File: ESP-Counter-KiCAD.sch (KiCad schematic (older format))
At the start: 37 parts, among them J1 Digital_IP, J2 Motor_Ctrl, J3 LED_Indicator, J5 24V_Input, K2 G2RL-1-DC24, K5 G2RL-1-DC24, U1 ESP_12E_J1, U10 VO615A, U2 ESP_12E_J2, U3 VO615A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

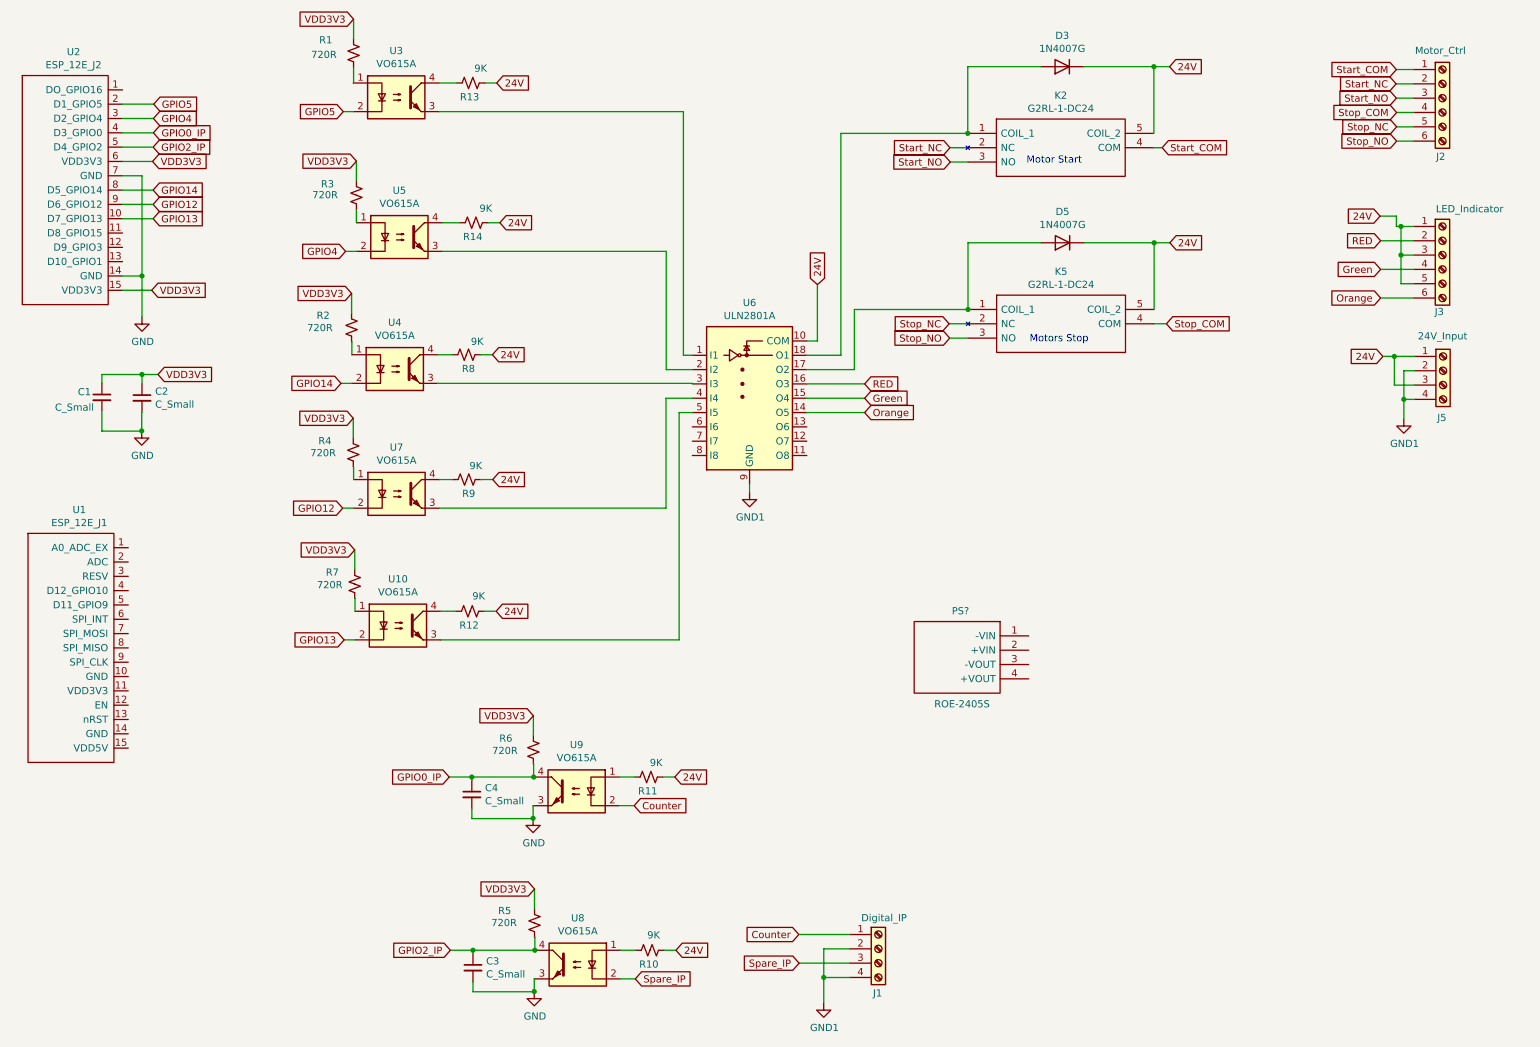
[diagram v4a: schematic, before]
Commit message: RECOM DCDC connections completed
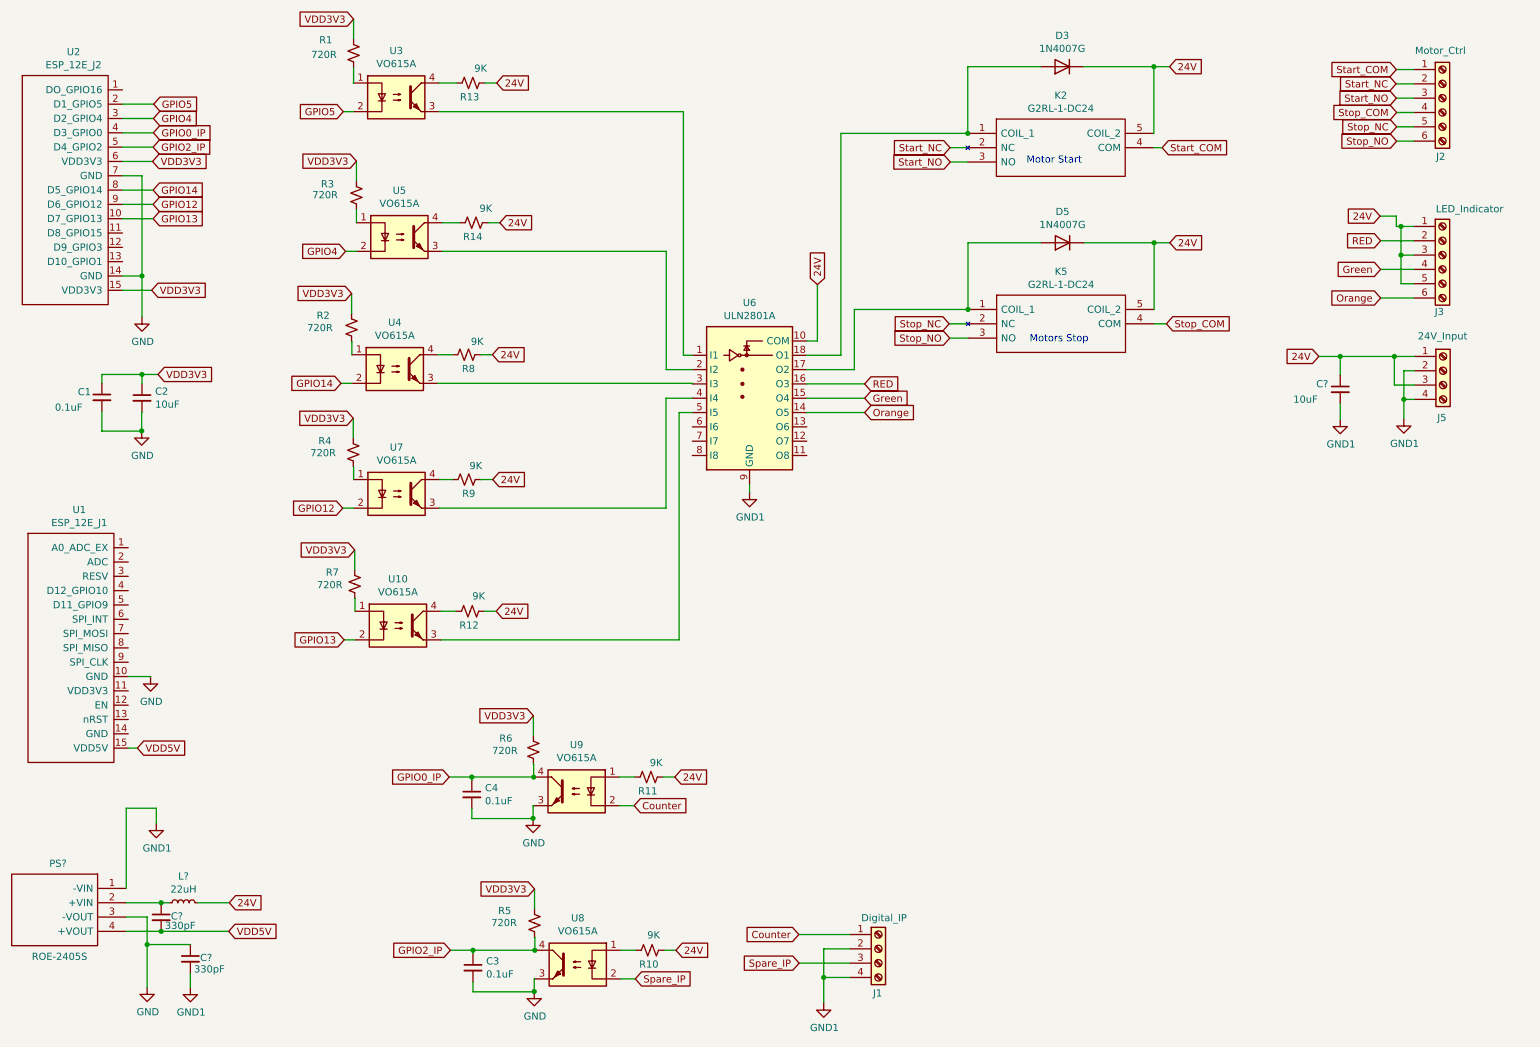
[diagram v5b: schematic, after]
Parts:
- added C?: 10uF, Capacitor_SMD:C_0603_1608Metric_Pad1.08x0.95mm_HandSolder, symbol Device:C_Small
- added C? (x2): 330pF, Capacitor_SMD:C_0603_1608Metric_Pad1.08x0.95mm_HandSolder, symbol Device:C_Small
- added L?: 22uH, symbol Device:L_Small
- C1, C3, C4: value C_Small -> 0.1uF
- C2: value C_Small -> 10uF
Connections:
- net labels added: VDD5V
- wire segments 152 -> 174
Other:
- moved on the sheet: PS?
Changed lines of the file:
@@
 P 1596 3302
 F 0 "C2" H 1688 3348 50  0000 L CNN
-F 1 "C_Small" H 1688 3257 50  0000 L CNN
+F 1 "10uF" H 1688 3257 50  0000 L CNN
 F 2 "Capacitor_SMD:C_0603_1608Metric_Pad1.08x0.95mm_HandSolder" H 1596 3302 50  0001 C CNN
 F 3 "~" H 1596 3302 50  0001 C CNN
@@
 P 1316 3298
 F 0 "C1" H 1148 3336 50  0000 L CNN
-F 1 "C_Small" H 988 3228 50  0000 L CNN
+F 1 "0.1uF" H 988 3228 50  0000 L CNN
 F 2 "Capacitor_SMD:C_0603_1608Metric_Pad1.08x0.95mm_HandSolder" H 1316 3298 50  0001 C CNN
 F 3 "~" H 1316 3298 50  0001 C CNN
@@
 	1    0    0    -1
 $EndComp
-Text GLabel 10264 3012 0    50   Input ~ 0
+Text GLabel 9816 3012 0    50   Input ~ 0
 24V
 Wire Wire Line
-	10264 3012 10344 3012
-Wire Wire Line
 	10484 3212 10344 3212
 Wire Wire Line
 	10344 3212 10344 3012
-Connection ~ 10344 3012
 Wire Wire Line
 	10344 3012 10484 3012
@@
 P 3900 6072
 F 0 "C4" H 3992 6118 50  0000 L CNN
-F 1 "C_Small" H 3992 6027 50  0000 L CNN
+F 1 "0.1uF" H 3992 6027 50  0000 L CNN
 F 2 "Capacitor_SMD:C_0603_1608Metric_Pad1.08x0.95mm_HandSolder" H 3900 6072 50  0001 C CNN
 F 3 "~" H 3900 6072 50  0001 C CNN
@@
 P 3908 7282
 F 0 "C3" H 4000 7328 50  0000 L CNN
-F 1 "C_Small" H 4000 7237 50  0000 L CNN
+F 1 "0.1uF" H 4000 7237 50  0000 L CNN
 F 2 "Capacitor_SMD:C_0603_1608Metric_Pad1.08x0.95mm_HandSolder" H 3908 7282 50  0001 C CNN
 F 3 "~" H 3908 7282 50  0001 C CNN
@@
 L ROE-2405S:ROE-2405S PS?
 U 1 1 601CB8A2
-P 7790 4964
-F 0 "PS?" H 8206 5138 50  0000 L CNN
-F 1 "ROE-2405S" H 8062 4488 50  0000 L CNN
-F 2 "ROE1205S" H 8640 5064 50  0001 L CNN
-F 3 "https://recom-power.com/pdf/Econoline/ROE.pdf" H 8640 4964 50  0001 L CNN
-F 4 "Recom Through Hole 1W Isolated DC-DC Converter, I/O isolation 1kV dc, Vout 5V dc" H 8640 4864 50  0001 L CNN "Description"
-F 5 "10.5" H 8640 4764 50  0001 L CNN "Height"
-F 6 "RECOM Power" H 8640 4664 50  0001 L CNN "Manufacturer_Name"
-F 7 "ROE-2405S" H 8640 4564 50  0001 L CNN "Manufacturer_Part_Number"
-F 8 "919-ROE-2405S" H 8640 4464 50  0001 L CNN "Mouser Part Number"
-F 9 "https://www.mouser.co.uk/ProductDetail/RECOM-Power/ROE-2405S/?qs=wlO1EFRhkBD1PQdCwpEhnw%3D%3D" H 8640 4364 50  0001 L CNN "Mouser Price/Stock"
-F 10 "ROE-2405S" H 8640 4264 50  0001 L CNN "Arrow Part Number"
-F 11 "https://www.arrow.com/en/products/roe-2405s/recom-power" H 8640 4164 50  0001 L CNN "Arrow Price/Stock"
-	1    7790 4964
+P 1486 6728
+F 0 "PS?" H 1902 6902 50  0000 L CNN
+F 1 "ROE-2405S" H 1758 6252 50  0000 L CNN
+F 2 "ROE1205S" H 2336 6828 50  0001 L CNN
+F 3 "https://recom-power.com/pdf/Econoline/ROE.pdf" H 2336 6728 50  0001 L CNN
+F 4 "Recom Through Hole 1W Isolated DC-DC Converter, I/O isolation 1kV dc, Vout 5V dc" H 2336 6628 50  0001 L CNN "Description"
+F 5 "10.5" H 2336 6528 50  0001 L CNN "Height"
+F 6 "RECOM Power" H 2336 6428 50  0001 L CNN "Manufacturer_Name"
+F 7 "ROE-2405S" H 2336 6328 50  0001 L CNN "Manufacturer_Part_Number"
+F 8 "919-ROE-2405S" H 2336 6228 50  0001 L CNN "Mouser Part Number"
+F 9 "https://www.mouser.co.uk/ProductDetail/RECOM-Power/ROE-2405S/?qs=wlO1EFRhkBD1PQdCwpEhnw%3D%3D" H 2336 6128 50  0001 L CNN "Mouser Price/Stock"
+F 10 "ROE-2405S" H 2336 6028 50  0001 L CNN "Arrow Part Number"
+F 11 "https://www.arrow.com/en/products/roe-2405s/recom-power" H 2336 5928 50  0001 L CNN "Arrow Price/Stock"
+	1    1486 6728
 	-1   0    0    -1
 $EndComp
@@
 Wire Wire Line
 	10390 2304 10390 2504
+Wire Wire Line
+	9816 3012 9966 3012
+Wire Wire Line
+	10344 3012 10344 3014
+Connection ~ 10344 3012
+$Comp
+L Device:C_Small C?
+U 1 1 6026B2BA
+P 9966 3242
+F 0 "C?" H 9798 3280 50  0000 L CNN
+F 1 "10uF" H 9638 3172 50  0000 L CNN
+F 2 "Capacitor_SMD:C_0603_1608Metric_Pad1.08x0.95mm_HandSolder" H 9966 3242 50  0001 C CNN
+F 3 "~" H 9966 3242 50  0001 C CNN
+	1    9966 3242
+	1    0    0    -1
+$EndComp
+$Comp
+L power:GND1 #PWR?
+U 1 1 6026C34F
+P 9966 3452
+F 0 "#PWR?" H 9966 3202 50  0001 C CNN
+F 1 "GND1" H 9971 3279 50  0000 C CNN
+F 2 "" H 9966 3452 50  0001 C CNN
+F 3 "" H 9966 3452 50  0001 C CNN
+	1    9966 3452
+	1    0    0    -1
+$EndComp
+Wire Wire Line
+	9966 3452 9966 3342
+Wire Wire Line
+	9966 3012 9966 3142
+Connection ~ 9966 3012
+Wire Wire Line
+	9966 3012 10344 3012
+Text GLabel 2206 6828 2    50   Input ~ 0
+24V
+$Comp
+L Device:L_Small L?
+U 1 1 6027A5EF
+P 1886 6828
+F 0 "L?" V 2071 6828 50  0000 C CNN
+F 1 "22uH" V 1980 6828 50  0000 C CNN
+F 2 "" H 1886 6828 50  0001 C CNN
+F 3 "~" H 1886 6828 50  0001 C CNN
+	1    1886 6828
+	0    -1   -1   0
+$EndComp
+Wire Wire Line
+	1486 6828 1730 6828
+Wire Wire Line
+	1986 6828 2206 6828
+Text GLabel 2202 7028 2    50   Input ~ 0
+VDD5V
+Wire Wire Line
+	1486 7028 1730 7028
+$Comp
+L power:GND #PWR?
+U 1 1 602955C8
+P 1632 7418
+F 0 "#PWR?" H 1632 7168 50  0001 C CNN
+F 1 "GND" H 1637 7245 50  0000 C CNN
+F 2 "" H 1632 7418 50  0001 C CNN
+F 3 "" H 1632 7418 50  0001 C CNN
+	1    1632 7418
+	1    0    0    -1
+$EndComp
+Wire Wire Line
+	1486 6928 1632 6928
+Wire Wire Line
+	1632 6928 1632 7120
+$Comp
+L power:GND1 #PWR?
+U 1 1 6029D955
+P 1696 6274
+F 0 "#PWR?" H 1696 6024 50  0001 C CNN
+F 1 "GND1" H 1701 6101 50  0000 C CNN
+F 2 "" H 1696 6274 50  0001 C CNN
+F 3 "" H 1696 6274 50  0001 C CNN
+	1    1696 6274
+	1    0    0    -1
+$EndComp
+Wire Wire Line
+	1486 6728 1486 6168
+Wire Wire Line
+	1486 6168 1696 6168
+Wire Wire Line
+	1696 6168 1696 6274
+Wire Wire Line
+	1730 7032 1730 7028
+Connection ~ 1730 7028
+Wire Wire Line
+	1730 7028 2202 7028
+Wire Wire Line
+	1730 6828 1730 6830
+Connection ~ 1730 6828
+Wire Wire Line
+	1730 6828 1786 6828
+$Comp
+L Device:C_Small C?
+U 1 1 602A61AB
+P 1730 6930
+F 0 "C?" H 1798 6938 50  0000 L CNN
+F 1 "330pF" H 1756 6872 50  0000 L CNN
+F 2 "Capacitor_SMD:C_0603_1608Metric_Pad1.08x0.95mm_HandSolder" H 1730 6930 50  0001 C CNN
+F 3 "~" H 1730 6930 50  0001 C CNN
+	1    1730 6930
+	1    0    0    -1
+$EndComp
+$Comp
+L Device:C_Small C?
+U 1 1 602B8471
+P 1934 7220
+F 0 "C?" H 2002 7228 50  0000 L CNN
+F 1 "330pF" H 1960 7148 50  0000 L CNN
+F 2 "Capacitor_SMD:C_0603_1608Metric_Pad1.08x0.95mm_HandSolder" H 1934 7220 50  0001 C CNN
+F 3 "~" H 1934 7220 50  0001 C CNN
+	1    1934 7220
+	1    0    0    -1
+$EndComp
+$Comp
+L power:GND1 #PWR?
+U 1 1 602B89B8
+P 1934 7420
+F 0 "#PWR?" H 1934 7170 50  0001 C CNN
+F 1 "GND1" H 1939 7247 50  0000 C CNN
+F 2 "" H 1934 7420 50  0001 C CNN
+F 3 "" H 1934 7420 50  0001 C CNN
+	1    1934 7420
+	1    0    0    -1
+$EndComp
+Wire Wire Line
+	1934 7120 1632 7120
+Connection ~ 1632 7120
+Wire Wire Line
+	1632 7120 1632 7418
+Wire Wire Line
+	1934 7420 1934 7320
+Text GLabel 1564 5748 2    50   Input ~ 0
+VDD5V
+Wire Wire Line
+	1500 5748 1564 5748
+$Comp
+L power:GND #PWR?
+U 1 1 602E7FBB
+P 1656 5250
+F 0 "#PWR?" H 1656 5000 50  0001 C CNN
+F 1 "GND" H 1661 5077 50  0000 C CNN
+F 2 "" H 1656 5250 50  0001 C CNN
+F 3 "" H 1656 5250 50  0001 C CNN
+	1    1656 5250
+	1    0    0    -1
+$EndComp
+Wire Wire Line
+	1500 5248 1656 5248
+Wire Wire Line
+	1656 5248 1656 5250
 $EndSCHEMATC

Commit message: EEPROM added to schematic
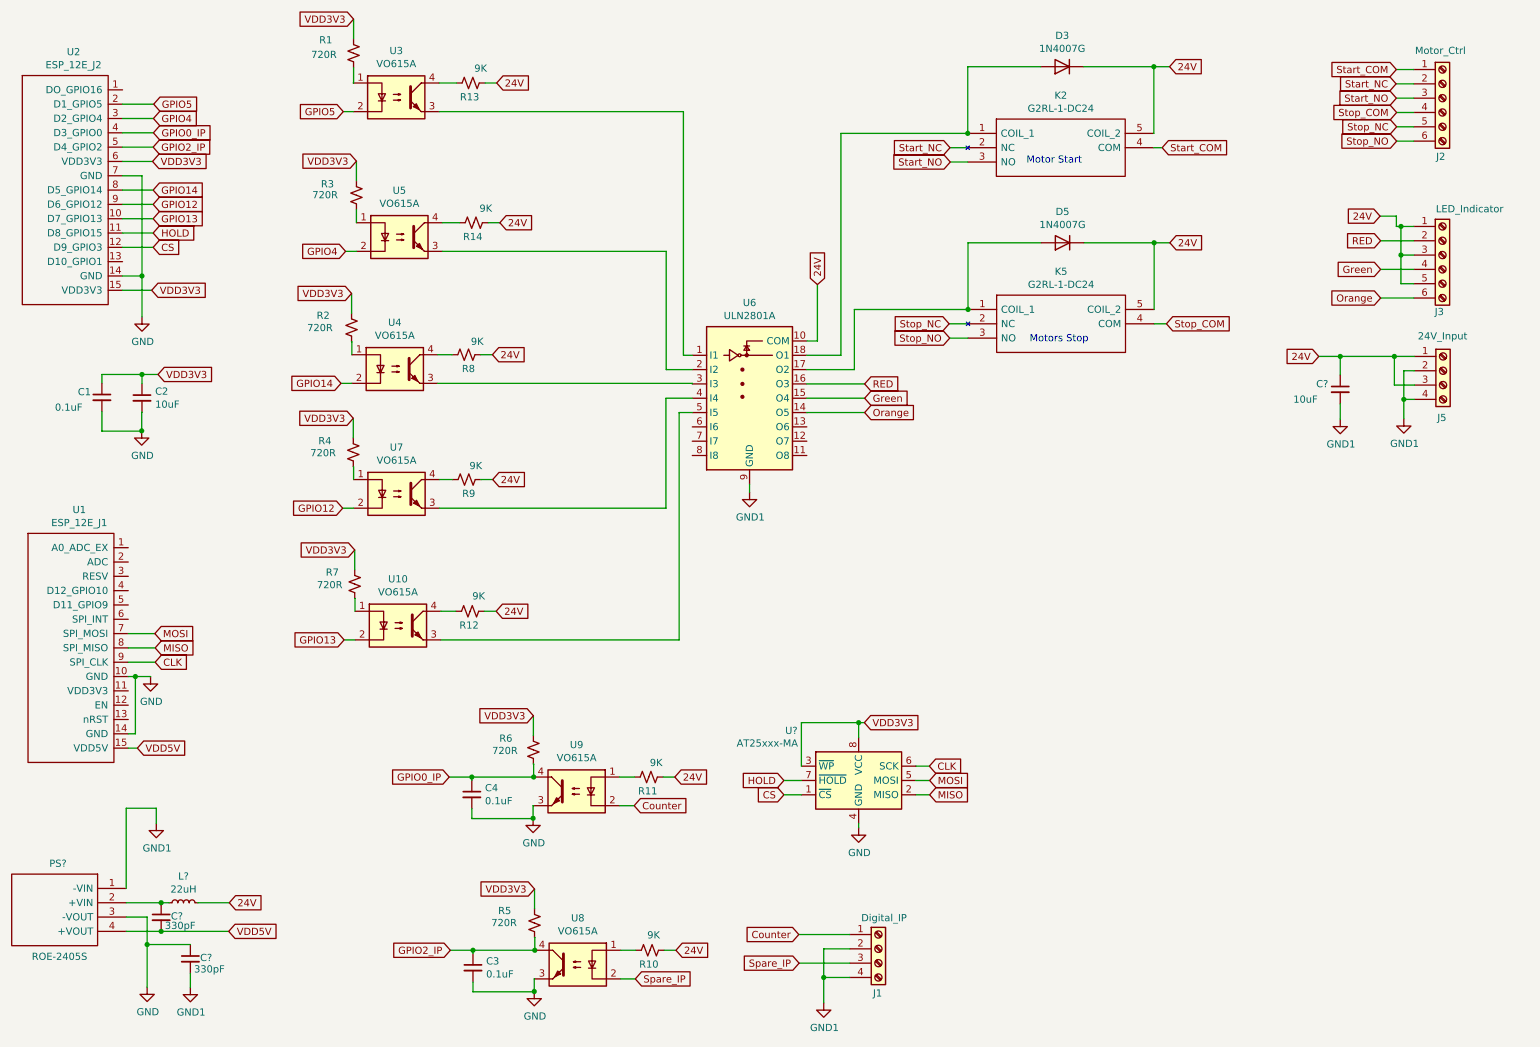
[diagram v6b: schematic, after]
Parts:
- added U?: AT25xxx-MA, Package_DFN_QFN:DFN-8-1EP_3x2mm_P0.5mm_EP1.75x1.45mm, symbol Memory_EEPROM:AT25xxx-MA
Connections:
- net labels added: CLK, CS, HOLD, MISO, MOSI
- wire segments 174 -> 192
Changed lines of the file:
@@
 $EndComp
 Wire Wire Line
-	1500 5248 1656 5248
+	1656 5248 1656 5250
+$Comp
+L Memory_EEPROM:AT25xxx-MA U?
+U 1 1 6025A0E8
+P 6602 5974
+F 0 "U?" H 6132 6322 50  0000 C CNN
+F 1 "AT25xxx-MA" H 5964 6234 50  0000 C CNN
+F 2 "Package_DFN_QFN:DFN-8-1EP_3x2mm_P0.5mm_EP1.75x1.45mm" H 6602 5974 50  0001 C CNN
+F 3 "http://ww1.microchip.com/downloads/en/DeviceDoc/Atmel-8707-SEEPROM-AT25010B-020B-040B-Datasheet.pdf" H 6602 5974 50  0001 C CNN
+	1    6602 5974
+	1    0    0    -1
+$EndComp
+Text GLabel 6642 5570 2    50   Input ~ 0
+VDD3V3
 Wire Wire Line
-	1656 5248 1656 5250
+	6602 5674 6602 5570
+Wire Wire Line
+	6202 5874 6202 5570
+Wire Wire Line
+	6202 5570 6602 5570
+Connection ~ 6602 5570
+Wire Wire Line
+	6602 5570 6642 5570
+$Comp
+L power:GND #PWR?
+U 1 1 6027DABC
+P 6602 6306
+F 0 "#PWR?" H 6602 6056 50  0001 C CNN
+F 1 "GND" H 6607 6133 50  0000 C CNN
+F 2 "" H 6602 6306 50  0001 C CNN
+F 3 "" H 6602 6306 50  0001 C CNN
+	1    6602 6306
+	1    0    0    -1
+$EndComp
+Wire Wire Line
+	6602 6306 6602 6274
+Text GLabel 1686 4948 2    50   Input ~ 0
+MOSI
+Wire Wire Line
+	1500 4948 1686 4948
+Text GLabel 1688 5048 2    50   Input ~ 0
+MISO
+Wire Wire Line
+	1500 5048 1688 5048
+Text GLabel 7098 5974 2    50   Input ~ 0
+MOSI
+Wire Wire Line
+	7002 5974 7098 5974
+Text GLabel 7098 6074 2    50   Input ~ 0
+MISO
+Wire Wire Line
+	7002 6074 7098 6074
+Text GLabel 1688 5148 2    50   Input ~ 0
+CLK
+Wire Wire Line
+	1500 5148 1688 5148
+Text GLabel 7096 5874 2    50   Input ~ 0
+CLK
+Wire Wire Line
+	7002 5874 7096 5874
+Text GLabel 1674 2150 2    50   Input ~ 0
+HOLD
+Text GLabel 1674 2250 2    50   Input ~ 0
+CS
+Wire Wire Line
+	1460 2150 1674 2150
+Wire Wire Line
+	1460 2250 1674 2250
+Text GLabel 6080 5974 0    50   Input ~ 0
+HOLD
+Wire Wire Line
+	6080 5974 6202 5974
+Text GLabel 6080 6074 0    50   Input ~ 0
+CS
+Wire Wire Line
+	6080 6074 6202 6074
+Wire Wire Line
+	1500 5648 1550 5648
+Wire Wire Line
+	1550 5648 1550 5248
+Wire Wire Line
+	1500 5248 1550 5248
+Connection ~ 1550 5248
+Wire Wire Line
+	1550 5248 1656 5248
 $EndSCHEMATC
